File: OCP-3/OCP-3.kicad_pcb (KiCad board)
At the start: 2 copper layers, 90 x 100 mm, 183 parts, among them X1 ico*отверстие*М3, X2 ico*отверстие*М3, X3 ico*отверстие*М3, X4 ico*отверстие*М3, X5 ico*LOGO_NIKITOS_10х10

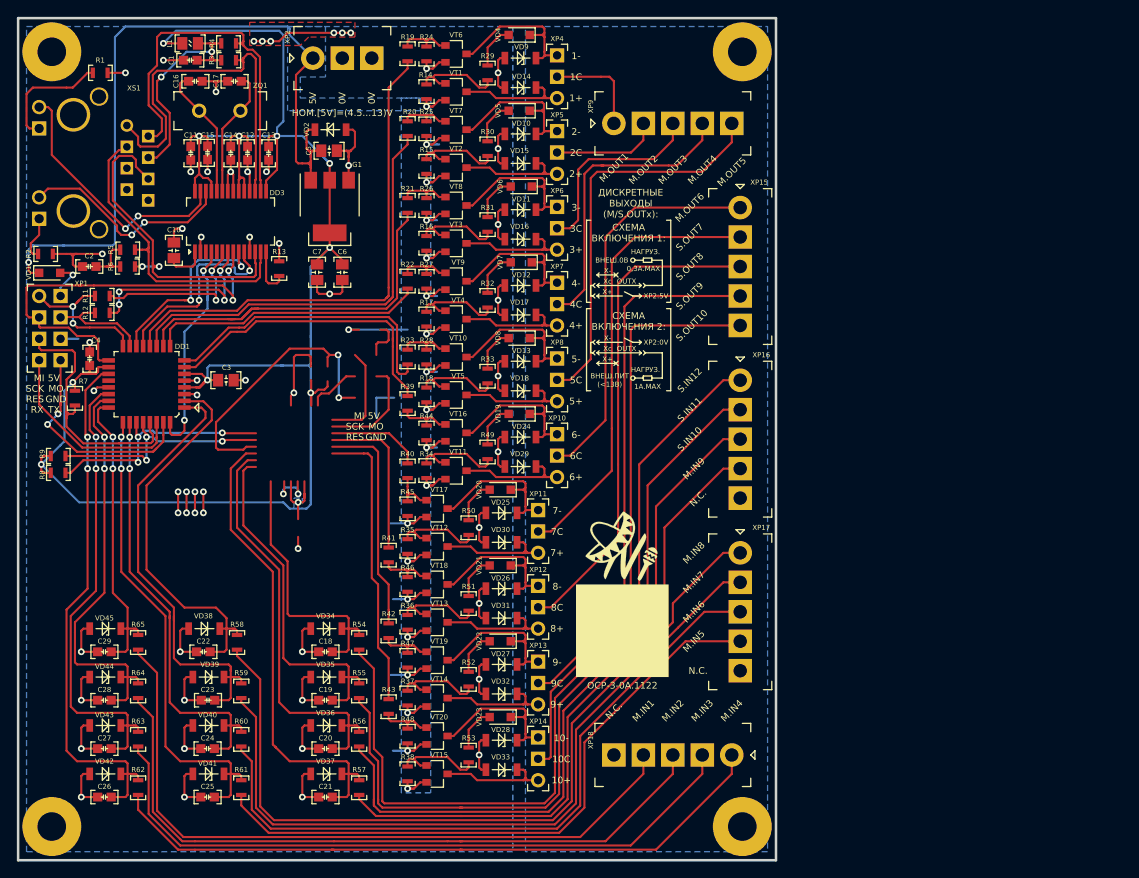
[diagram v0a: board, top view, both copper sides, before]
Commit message: на схему вынесены транзисторы
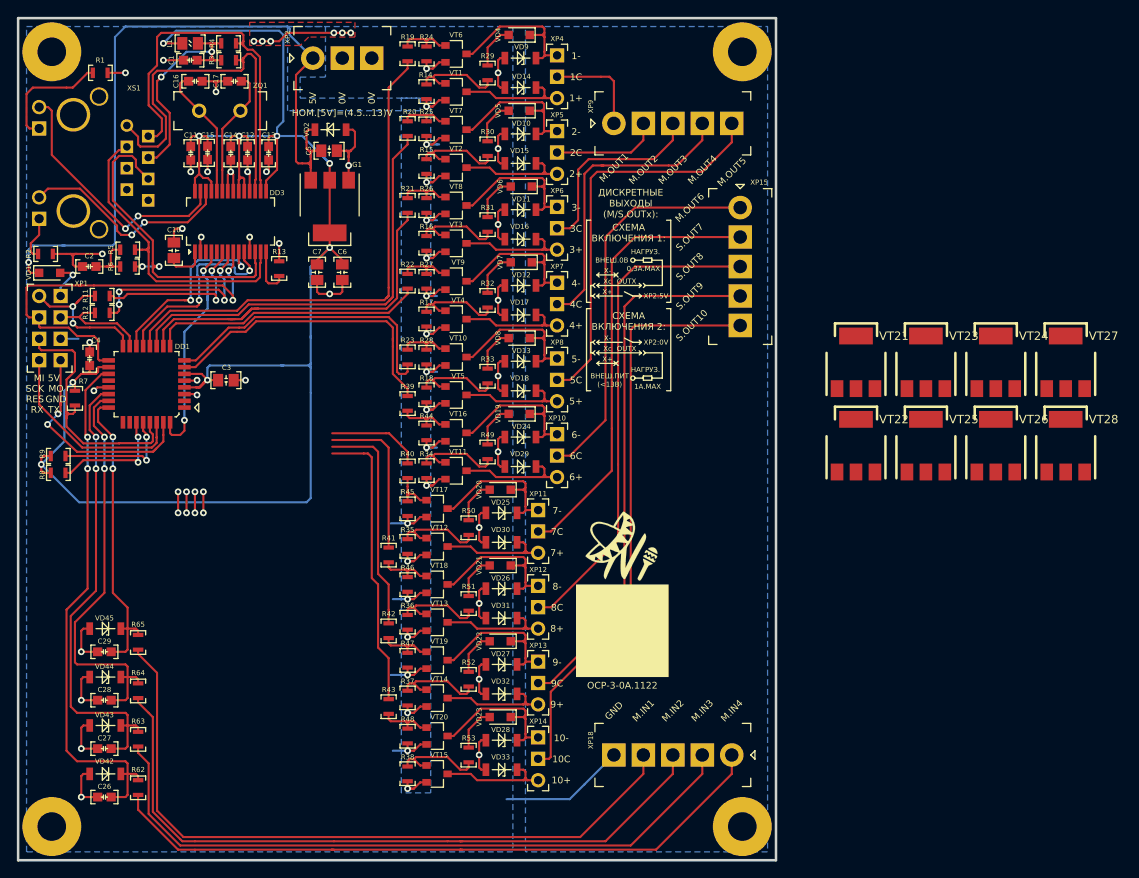
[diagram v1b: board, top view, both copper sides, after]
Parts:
- removed C18, C19, C20, C21, C22, C23, C24, C25: Конденсатор*0,1мкФ*25В*0603, N_RLC:Конденсатор_SMD_IEC_0603
- removed R54, R55, R56, R57, R58, R59, R60, R61: Резистор*1кОм*0603, N_RLC:Резистор_SMD_0603_0,065_Вт_pnp
- removed VD34, VD35, VD36, VD37, VD38, VD39, VD40, VD41: Стабилитрон*3,9В*SOD80, N_VD_HL:SOD-80
- removed XP16, XP17: Клеммник*шаг_3,5*5контактов*1ряд*вертикальная, N_X:Клеммник_15EDGVC-3.5-05P
- added VT21: Транзистор_NPN_1Б-2(4)К-3Э_0, N_VD_HL:Транзистор_NPN_SOT223, F.Cu at (149.5, 90.2)
- added VT22: Транзистор_NPN_1Б-2(4)К-3Э_0, N_VD_HL:Транзистор_NPN_SOT223, F.Cu at (149.5, 100.2)
- added VT23: Транзистор_NPN_1Б-2(4)К-3Э_0, N_VD_HL:Транзистор_NPN_SOT223, F.Cu at (157.8, 90.2)
- added VT24: Транзистор_NPN_1Б-2(4)К-3Э_0, N_VD_HL:Транзистор_NPN_SOT223, F.Cu at (166.1, 90.2)
- added VT25: Транзистор_NPN_1Б-2(4)К-3Э_0, N_VD_HL:Транзистор_NPN_SOT223, F.Cu at (157.8, 100.2)
- added VT26: Транзистор_NPN_1Б-2(4)К-3Э_0, N_VD_HL:Транзистор_NPN_SOT223, F.Cu at (166.1, 100.2)
- added VT27: Транзистор_NPN_1Б-2(4)К-3Э_0, N_VD_HL:Транзистор_NPN_SOT223, F.Cu at (174.4, 90.2)
- added VT28: Транзистор_NPN_1Б-2(4)К-3Э_0, N_VD_HL:Транзистор_NPN_SOT223, F.Cu at (174.4, 100.2)
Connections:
- XP18 pad 5: Net-(XP18-Pad5) -> GND
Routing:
- net /DIN12: track 99.5 -> 0.00 mm
- net /DIN8: track 97.3 -> 0.00 mm
- net /DIN11: track 92.0 -> 0.00 mm
- net /DIN7: track 89.1 -> 0.00 mm
- net /DIN10: track 84.4 -> 0.00 mm
- net /DIN6: track 82.4 -> 0.00 mm
- net /DIN9: track 76.1 -> 0.00 mm
- net /DIN5: track 75.8 -> 0.00 mm
- net /MC.DIN5: track 57.7 -> 0.00 mm, vias 2 -> 0
- net /MC.DIN9: track 57.1 -> 0.00 mm
- net /MC.DIN7: track 53.4 -> 0.00 mm
- net /MC.DIN6: track 51.7 -> 0.00 mm, vias 2 -> 0
- net GND: track 272.7 -> 221.6 mm, vias 70 -> 58
- net /MC.DIN10: track 49.6 -> 0.00 mm
- net /MC.DIN8: track 46.2 -> 0.00 mm
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- removed copper zone on B.Cu, net 3V3
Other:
- board text removed: "M.IN5"
- board text removed: "M.IN6"
- board text removed: "M.IN7"
- board text removed: "M.IN8"
- board text removed: "M.IN9"
- board text removed: "N.C."
- board text removed: "S.IN10"
- board text removed: "S.IN11"
- board text removed: "S.IN12"
